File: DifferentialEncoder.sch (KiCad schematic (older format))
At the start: 8 parts, among them J1 Conn_02x04_Odd_Even, J2 ODrive Connector, U1 MAX3284E, U2 MAX3284E, U3 MAX3284E

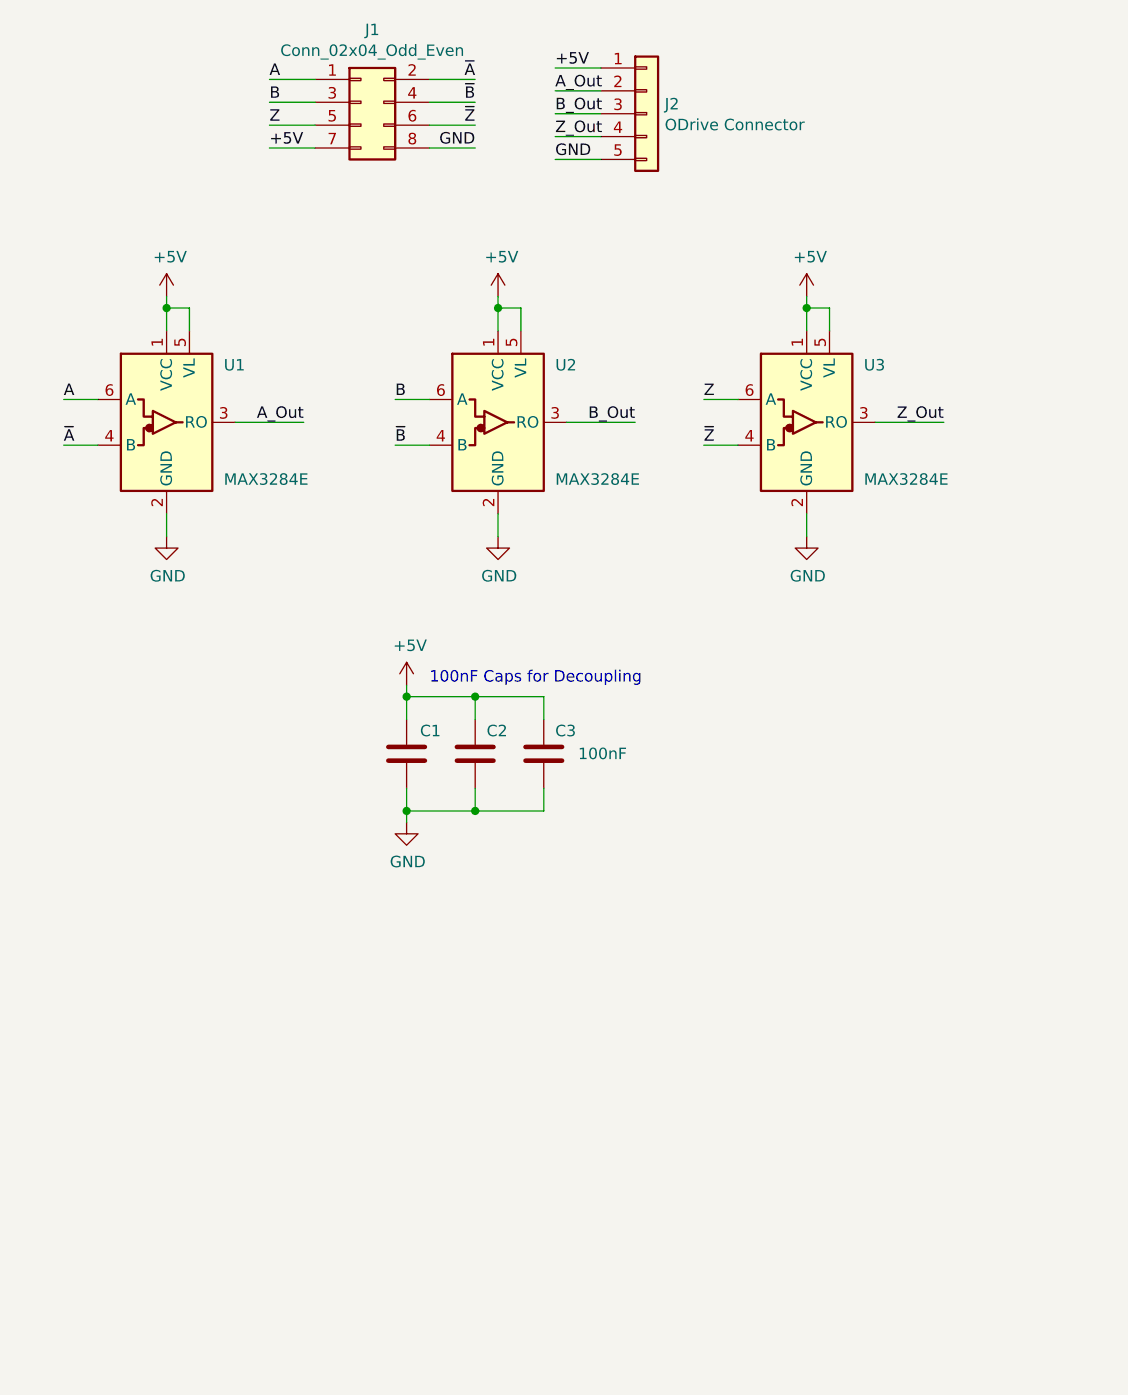
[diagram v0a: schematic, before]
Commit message: Update differential adapter with termination etc.
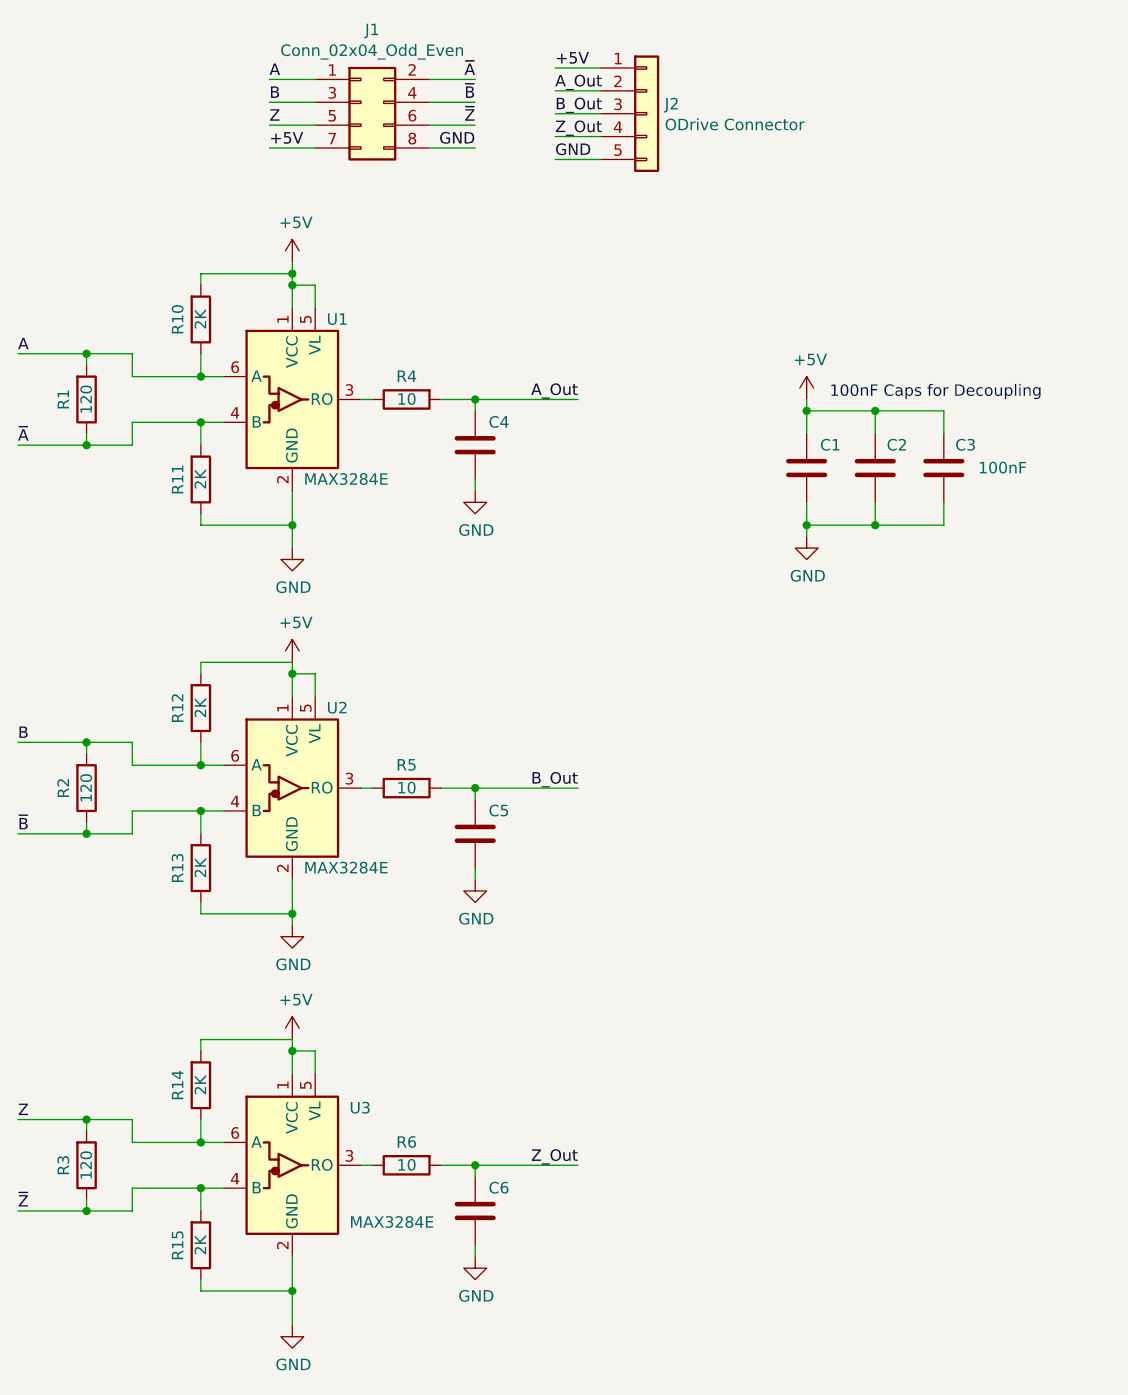
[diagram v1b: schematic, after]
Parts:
- added C4, C5, C6: 1nF, Capacitor_SMD:C_0805_2012Metric, symbol Device:C
- added R1, R2, R3: 120, Resistor_SMD:R_0805_2012Metric_Pad1.15x1.40mm_HandSolder, symbol Device:R
- added R10, R11, R12, R13, R14, R15: 2K, Resistor_SMD:R_0805_2012Metric_Pad1.15x1.40mm_HandSolder, symbol Device:R
- added R4, R5, R6: 10, Resistor_SMD:R_0805_2012Metric_Pad1.15x1.40mm_HandSolder, symbol Device:R
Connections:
- net +5V: now also R10.2, R12.2, R14.2
- net A: now also R1.2, R10.1
- net A_Out: now also C4.1, R4.2; no longer U1.3 (RO)
- net B: now also R12.1, R2.2
- net B_Out: now also C5.1, R5.2; no longer U2.3 (RO)
- net GND: now also C4.2, C5.2, C6.2, R11.1, R13.1, R15.1
- net Z: now also R14.1, R3.2
- net Z_Out: now also C6.1, R6.2; no longer U3.3 (RO)
- net ~A: now also R1.1, R11.2
- net ~B: now also R13.2, R2.1
- net ~Z: now also R15.2, R3.1
- new net: R4.1, U1.3 (RO)
- new net: R5.1, U2.3 (RO)
- new net: R6.1, U3.3 (RO)
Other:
- moved on the sheet: C1, C2, C3, U1, U2, U3
